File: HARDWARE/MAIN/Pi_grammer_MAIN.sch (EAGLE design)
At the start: 29 parts, among them J2 TARGET_copy, U1 AT42QT1010SOT23

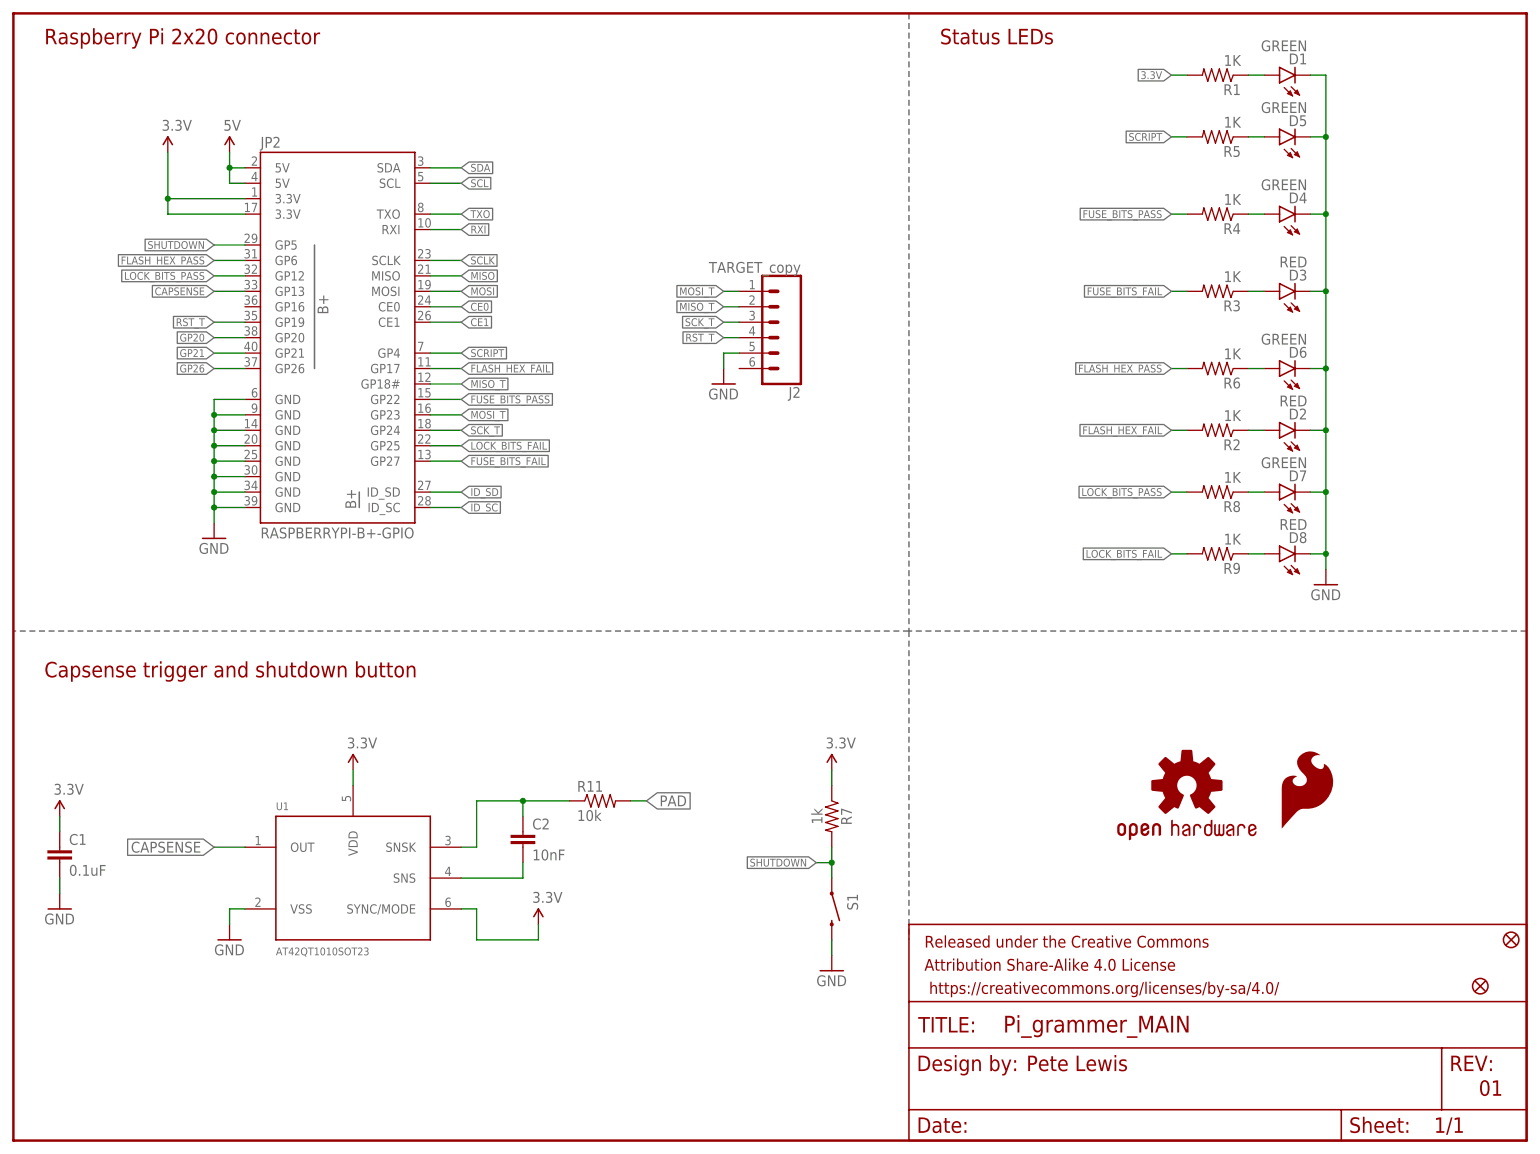
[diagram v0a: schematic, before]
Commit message: SPI pins and llc
Just SCH work at this point.
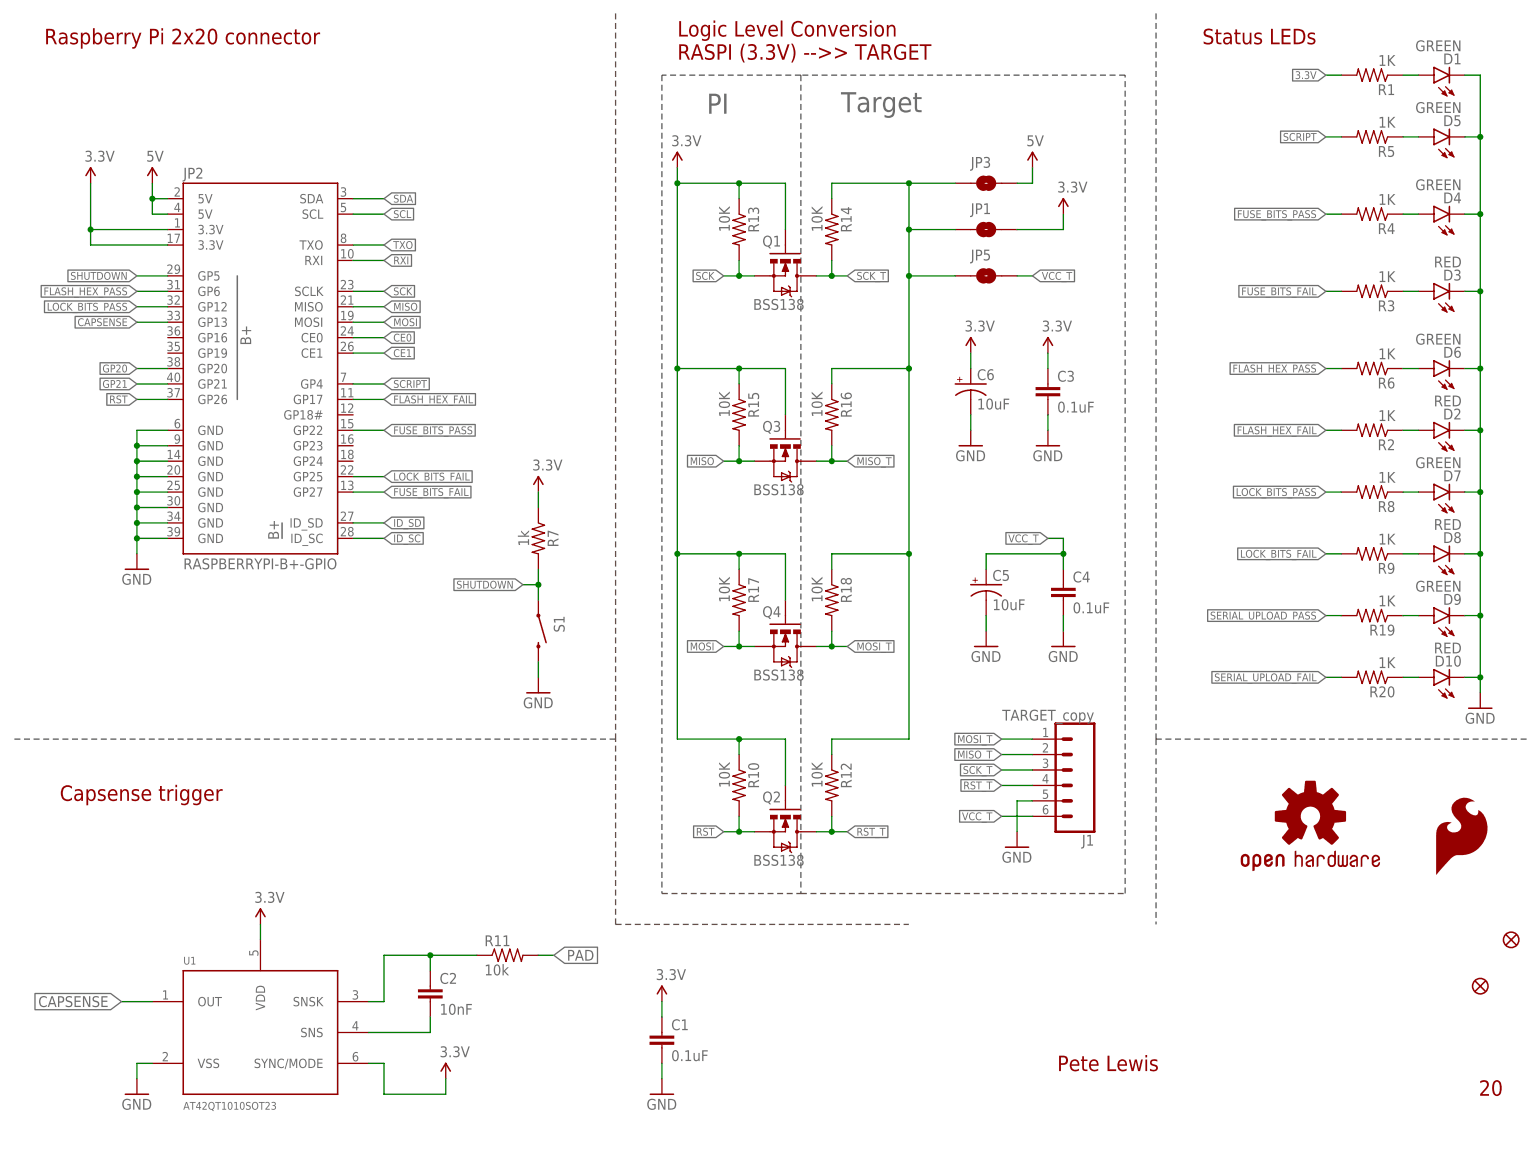
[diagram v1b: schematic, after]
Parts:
- removed FRAME1: FRAME-LETTER, SparkFun-Aesthetics:FRAME-LETTER
- removed J2: TARGET_copy, SparkFun-Connectors:CONN_06POLAR
- added C3, C4: 0.1uF, SparkFun-Capacitors:0.1UF-0603-25V-(+80/-20%)
- added C5, C6: 10uF, SparkFun-Capacitors:10UF-POLAR-EIA3216-16V-10%(TANT)
- added D10: RED, SparkFun-LED:LED-RED1206
- added D9: GREEN, SparkFun-LED:LED-GREEN1206
- added J1: TARGET_copy, SparkFun-Connectors:CONN_06SIP_LOCK
- added JP1, JP3, JP5: JUMPER-SMT_2_NO_SILK, SparkFun-Jumpers:JUMPER-SMT_2_NO_SILK
- added Q1, Q2, Q3, Q4: BSS138, SparkFun:MOSFET-NCHANNELSMD
- added R10, R12, R13, R14, R15, R16, R17, R18: 10K, SparkFun:RESISTOR0603-RES
- added R19, R20: 1K, SparkFun-Resistors:1KOHM-1/10W-1%(0603)
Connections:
- removed net GP26: JP2.GP26
- removed net SCLK: JP2.SCLK
- new net N$12: JP1.1, JP3.1, JP5.1, R12.1, R14.1, R16.1, R18.1
- new net N$13: D9.A, R19.1
- new net N$14: D10.A, R20.1
- new net RST: JP2.GP26, Q2.S, R10.2
- new net SCK: JP2.SCLK, Q1.S, R13.2
- new net SERIAL_UPLOAD_FAIL: R20.2
- new net SERIAL_UPLOAD_PASS: R19.2
- new net VCC_T: C4.1, C5.+, J1.6, JP5.2
- net 3.3V: now also C3.1, C6.+, JP1.2, Q1.G, Q2.G, Q3.G, Q4.G, R10.1, R13.1, R15.1, R17.1
- net 5V: now also JP3.2
- net GND: now also C3.2, C4.2, C5.-, C6.-, D10.C, D9.C, J1.5; no longer J2.5
- net MISO: now also Q3.S, R15.2
- net MISO_T: now also J1.2, Q3.D, R16.2; no longer J2.2, JP2.GP18#
- net MOSI: now also Q4.S, R17.2
- net MOSI_T: now also J1.1, Q4.D, R18.2; no longer J2.1, JP2.GP23
- net RST_T: now also J1.4, Q2.D, R12.2; no longer J2.4, JP2.GP19
- net SCK_T: now also J1.3, Q1.D, R14.2; no longer J2.3, JP2.GP24
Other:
- note added: "20"
- note added: "Capsense trigger"
- note added: "Logic Level Conversion RASPI (3.3V) -->> TARGET"
- note added: "PI"
- note added: "Target"
- note removed: "01"
- note removed: "Capsense trigger and shutdown button"
- moved on the sheet: C1, C2, D1, D2, D3, D4, D5, D6, D7, D8, JP2, R1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

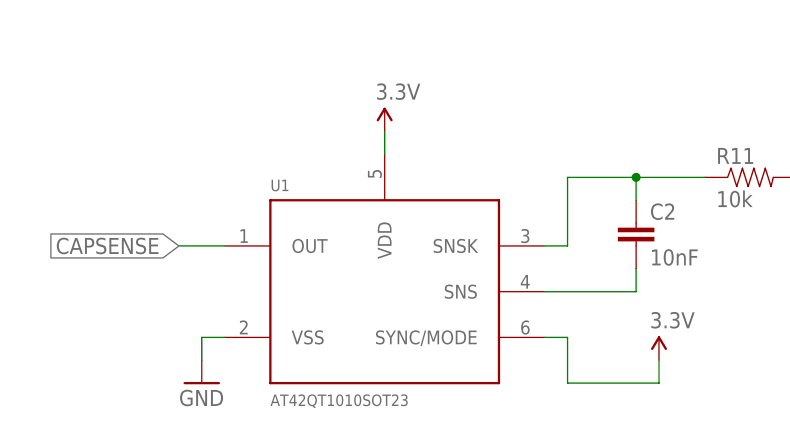
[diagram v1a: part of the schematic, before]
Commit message: capsense IC replacement
trying out the UDFN package - dang that's tiny
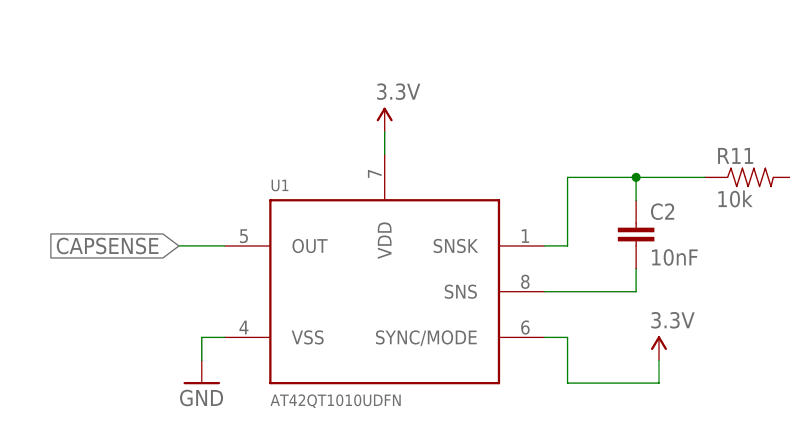
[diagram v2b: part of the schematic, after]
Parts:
- U1: value AT42QT1010SOT23 -> AT42QT1010UDFN; device SparkFun-DigitalIC:AT42QT1010SOT23 -> Testing:AT42QT1010UDFN
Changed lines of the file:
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@@
 <layer number="230" name="230bmp" color="7" fill="1" visible="yes" active="yes"/>
 <layer number="231" name="231bmp" color="7" fill="1" visible="yes" active="yes"/>
+<layer number="232" name="Eagle3D_PG2" color="7" fill="1" visible="yes" active="yes"/>
+<layer number="233" name="Eagle3D_PG3" color="7" fill="1" visible="yes" active="yes"/>
 <layer number="248" name="Housing" color="7" fill="1" visible="yes" active="yes"/>
 <layer number="249" name="Edge" color="7" fill="1" visible="yes" active="yes"/>
@@
 <part name="LOGO1" library="SparkFun-Aesthetics" deviceset="SFE_LOGO_FLAME" device=".1_INCH"/>
 <part name="LOGO2" library="SparkFun-Aesthetics" deviceset="OSHW-LOGO" device="S" value="OSHW-LOGOS"/>
-<part name="U1" library="SparkFun-DigitalIC" deviceset="AT42QT1010" device="SOT23">
+<part name="U1" library="Testing" deviceset="AT42QT1010" device="UDFN">
 <attribute name="PROD_ID" value="IC-11778"/>
 </part>

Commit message: finished layout v20
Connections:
- removed net N$12: JP1.1, JP3.1, JP5.1, R12.1, R14.1, R16.1, R18.1
- new net N$9: C4.1, C5.+, JP1.1, JP3.1, JP5.1, R12.1, R14.1, R16.1, R18.1
- net SERIAL_UPLOAD_FAIL: now also JP2.GP24
- net SERIAL_UPLOAD_PASS: now also JP2.GP23
- net VCC_T: no longer C4.1, C5.+
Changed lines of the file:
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@@
 <label x="175.26" y="325.12" size="1.27" layer="95" xref="yes"/>
 </segment>
+</net>
+<net name="N$13" class="0">
+<segment>
+<pinref part="D9" gate="G$1" pin="A"/>
+<pinref part="R19" gate="G$1" pin="1"/>
+<wire x1="238.76" y1="269.24" x2="236.22" y2="269.24" width="0.1524" layer="91"/>
+</segment>
+</net>
+<net name="N$14" class="0">
+<segment>
+<pinref part="D10" gate="G$1" pin="A"/>
+<pinref part="R20" gate="G$1" pin="1"/>
+<wire x1="238.76" y1="259.08" x2="236.22" y2="259.08" width="0.1524" layer="91"/>
+</segment>
+</net>
+<net name="SERIAL_UPLOAD_PASS" class="0">
+<segment>
+<pinref part="R19" gate="G$1" pin="2"/>
+<wire x1="226.06" y1="269.24" x2="223.52" y2="269.24" width="0.1524" layer="91"/>
+<label x="223.52" y="269.24" size="1.27" layer="95" rot="R180" xref="yes"/>
+</segment>
+<segment>
+<pinref part="JP2" gate="G$1" pin="GP23"/>
+<wire x1="63.5" y1="297.18" x2="68.58" y2="297.18" width="0.1524" layer="91"/>
+<label x="68.58" y="297.18" size="1.27" layer="95" xref="yes"/>
+</segment>
+</net>
+<net name="SERIAL_UPLOAD_FAIL" class="0">
+<segment>
+<pinref part="R20" gate="G$1" pin="2"/>
+<wire x1="226.06" y1="259.08" x2="223.52" y2="259.08" width="0.1524" layer="91"/>
+<label x="223.52" y="259.08" size="1.27" layer="95" rot="R180" xref="yes"/>
+</segment>
+<segment>
+<pinref part="JP2" gate="G$1" pin="GP24"/>
+<wire x1="63.5" y1="294.64" x2="68.58" y2="294.64" width="0.1524" layer="91"/>
+<label x="68.58" y="294.64" size="1.27" layer="95" xref="yes"/>
+</segment>
+</net>
+<net name="N$9" class="0">
 <segment>
 <pinref part="C4" gate="G$1" pin="1"/>
@@
 <pinref part="C5" gate="G$1" pin="+"/>
 <wire x1="167.64" y1="279.4" x2="167.64" y2="276.86" width="0.1524" layer="91"/>
-<wire x1="180.34" y1="279.4" x2="180.34" y2="281.94" width="0.1524" layer="91"/>
-<wire x1="180.34" y1="281.94" x2="177.8" y2="281.94" width="0.1524" layer="91"/>
-<junction x="180.34" y="279.4"/>
-<label x="177.8" y="281.94" size="1.27" layer="95" rot="R180" xref="yes"/>
-</segment>
-</net>
-<net name="N$12" class="0">
-<segment>
+<wire x1="167.64" y1="279.4" x2="157.48" y2="279.4" width="0.1524" layer="91"/>
+<wire x1="157.48" y1="279.4" x2="157.48" y2="281.94" width="0.1524" layer="91"/>
+<junction x="167.64" y="279.4"/>
 <pinref part="R12" gate="G$1" pin="1"/>
 <wire x1="142.24" y1="246.38" x2="142.24" y2="248.92" width="0.1524" layer="91"/>
@@
 <wire x1="154.94" y1="248.92" x2="154.94" y2="279.4" width="0.1524" layer="91"/>
 <pinref part="R18" gate="G$1" pin="1"/>
-<wire x1="154.94" y1="279.4" x2="154.94" y2="309.88" width="0.1524" layer="91"/>
+<wire x1="154.94" y1="279.4" x2="154.94" y2="281.94" width="0.1524" layer="91"/>
+<wire x1="154.94" y1="281.94" x2="154.94" y2="309.88" width="0.1524" layer="91"/>
 <wire x1="154.94" y1="309.88" x2="154.94" y2="325.12" width="0.1524" layer="91"/>
 <wire x1="154.94" y1="325.12" x2="154.94" y2="332.74" width="0.1524" layer="91"/>
@@
 <junction x="154.94" y="332.74"/>
 <junction x="154.94" y="325.12"/>
+<wire x1="157.48" y1="281.94" x2="154.94" y2="281.94" width="0.1524" layer="91"/>
+<junction x="154.94" y="281.94"/>
 </segment>
 </net>
-<net name="N$13" class="0">
-<segment>
-<pinref part="D9" gate="G$1" pin="A"/>
-<pinref part="R19" gate="G$1" pin="1"/>
-<wire x1="238.76" y1="269.24" x2="236.22" y2="269.24" width="0.1524" layer="91"/>
-</segment>
-</net>
-<net name="N$14" class="0">
-<segment>
-<pinref part="D10" gate="G$1" pin="A"/>
-<pinref part="R20" gate="G$1" pin="1"/>
-<wire x1="238.76" y1="259.08" x2="236.22" y2="259.08" width="0.1524" layer="91"/>
-</segment>
-</net>
-<net name="SERIAL_UPLOAD_PASS" class="0">
-<segment>
-<pinref part="R19" gate="G$1" pin="2"/>
-<wire x1="226.06" y1="269.24" x2="223.52" y2="269.24" width="0.1524" layer="91"/>
-<label x="223.52" y="269.24" size="1.27" layer="95" rot="R180" xref="yes"/>
-</segment>
-</net>
-<net name="SERIAL_UPLOAD_FAIL" class="0">
-<segment>
-<pinref part="R20" gate="G$1" pin="2"/>
-<wire x1="226.06" y1="259.08" x2="223.52" y2="259.08" width="0.1524" layer="91"/>
-<label x="223.52" y="259.08" size="1.27" layer="95" rot="R180" xref="yes"/>
-</segment>
-</net>

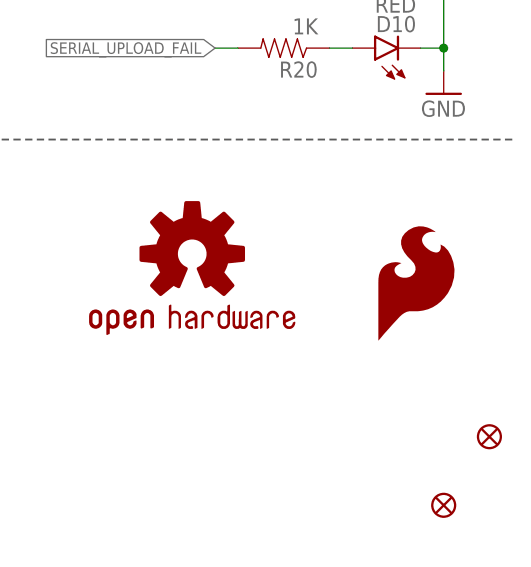
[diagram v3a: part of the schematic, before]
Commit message: updated SFE flame to proper polygon width dran package
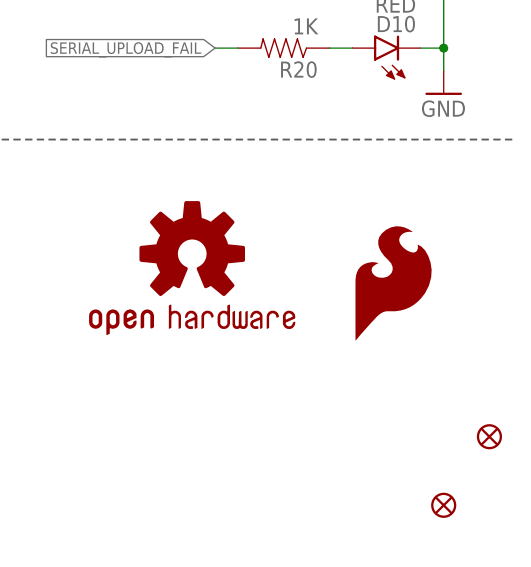
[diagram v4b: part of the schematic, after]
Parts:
- LOGO1: value SFE_LOGO_FLAME.1_INCH -> SFE_LOGO_FLAME.2_INCH; device SparkFun-Aesthetics:SFE_LOGO_FLAME.1_INCH -> SparkFun-Aesthetics:SFE_LOGO_FLAME.2_INCH
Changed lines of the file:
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@@
 <part name="R8" library="SparkFun-Resistors" deviceset="1KOHM-1/10W-1%(0603)" device="" value="1K"/>
 <part name="D7" library="SparkFun-LED" deviceset="LED-GREEN" device="1206" value="GREEN"/>
-<part name="LOGO1" library="SparkFun-Aesthetics" deviceset="SFE_LOGO_FLAME" device=".1_INCH"/>
 <part name="LOGO2" library="SparkFun-Aesthetics" deviceset="OSHW-LOGO" device="S" value="OSHW-LOGOS"/>
 <part name="U1" library="Testing" deviceset="AT42QT1010" device="UDFN">
@@
 <part name="C5" library="SparkFun-Capacitors" deviceset="10UF-POLAR" device="-EIA3216-16V-10%(TANT)" value="10uF"/>
 <part name="GND8" library="SparkFun-Aesthetics" deviceset="GND" device=""/>
+<part name="LOGO1" library="SparkFun-Aesthetics" deviceset="SFE_LOGO_FLAME" device=".2_INCH"/>
 </parts>
 <sheets>
@@
 <instance part="R8" gate="G$1" x="231.14" y="289.56" rot="R180"/>
 <instance part="D7" gate="G$1" x="241.3" y="289.56" rot="R90"/>
-<instance part="LOGO1" gate="G$1" x="241.3" y="226.06"/>
 <instance part="LOGO2" gate="G$1" x="220.98" y="236.22"/>
 <instance part="U1" gate="G$1" x="48.26" y="200.66">
@@
 <instance part="C5" gate="G$1" x="167.64" y="274.32"/>
 <instance part="GND8" gate="1" x="167.64" y="264.16"/>
+<instance part="LOGO1" gate="G$1" x="238.76" y="226.06"/>
 </instances>
 <busses>
